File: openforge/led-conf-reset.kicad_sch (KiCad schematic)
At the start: 48 parts, among them Q1 DDC114YU-7-F, Q2 DDC114YU-7-F

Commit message: added footprint associations
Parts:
- R55, R56, R57, R58, R59, R60, R61, R62, R63, R64, R65, R66, R67, R68, R69, R70, R71, R72, R73, R74, R75, R76, R77, R78, R79, R80, R81, R82, R83, R84, R85, R86, R87, R88, R89, R90, R91, R92, R93, R94, R95: footprint (none) -> Resistor_SMD:R_0402_1005Metric
- S2: footprint (none) -> footprints:KMR2xxG_CNK
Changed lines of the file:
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@@
 			)
 		)
-		(property "Footprint" ""
+		(property "Footprint" "Resistor_SMD:R_0402_1005Metric"
 			(at 328.93 93.472 90)
 			(effects
@@
 			)
 		)
-		(property "Footprint" ""
+		(property "Footprint" "Resistor_SMD:R_0402_1005Metric"
 			(at 100.838 119.38 90)
 			(effects
@@
 			)
 		)
-		(property "Footprint" ""
+		(property "Footprint" "Resistor_SMD:R_0402_1005Metric"
 			(at 108.712 46.99 90)
 			(effects
@@
 			)
 		)
-		(property "Footprint" ""
+		(property "Footprint" "Resistor_SMD:R_0402_1005Metric"
 			(at 66.802 46.99 90)
 			(effects
@@
 			)
 		)
-		(property "Footprint" ""
+		(property "Footprint" "Resistor_SMD:R_0402_1005Metric"
 			(at 93.472 46.99 90)
 			(effects
@@
 			)
 		)
-		(property "Footprint" ""
+		(property "Footprint" "Resistor_SMD:R_0402_1005Metric"
 			(at 120.142 46.99 90)
 			(effects
@@
 			)
 		)
-		(property "Footprint" ""
+		(property "Footprint" "Resistor_SMD:R_0402_1005Metric"
 			(at 74.168 119.38 90)
 			(effects
@@
 			)
 		)
-		(property "Footprint" ""
+		(property "Footprint" "Resistor_SMD:R_0402_1005Metric"
 			(at 116.332 46.99 90)
 			(effects
@@
 			)
 		)
-		(property "Footprint" ""
+		(property "Footprint" "Resistor_SMD:R_0402_1005Metric"
 			(at 116.078 119.38 90)
 			(effects
@@
 			)
 		)
-		(property "Footprint" ""
+		(property "Footprint" "Resistor_SMD:R_0402_1005Metric"
 			(at 82.042 46.99 90)
 			(effects
@@
 			)
 		)
-		(property "Footprint" ""
+		(property "Footprint" "Resistor_SMD:R_0402_1005Metric"
 			(at 127.508 119.38 90)
 			(effects
@@
 			)
 		)
-		(property "Footprint" ""
+		(property "Footprint" "Resistor_SMD:R_0402_1005Metric"
 			(at 292.862 48.26 90)
 			(effects
@@
 			)
 		)
-		(property "Footprint" ""
+		(property "Footprint" "Resistor_SMD:R_0402_1005Metric"
 			(at 89.662 46.99 90)
 			(effects
@@
 			)
 		)
-		(property "Footprint" ""
+		(property "Footprint" "Resistor_SMD:R_0402_1005Metric"
 			(at 252.73 97.028 90)
 			(effects
@@
 			)
 		)
-		(property "Footprint" ""
+		(property "Footprint" "Resistor_SMD:R_0402_1005Metric"
 			(at 119.888 119.38 90)
 			(effects
@@
 			)
 		)
-		(property "Footprint" ""
+		(property "Footprint" "Resistor_SMD:R_0402_1005Metric"
 			(at 112.522 46.99 90)
 			(effects
@@
 			)
 		)
-		(property "Footprint" ""
+		(property "Footprint" "Resistor_SMD:R_0402_1005Metric"
 			(at 112.268 119.38 90)
 			(effects
@@
 			)
 		)
-		(property "Footprint" ""
+		(property "Footprint" "Resistor_SMD:R_0402_1005Metric"
 			(at 369.062 48.26 90)
 			(effects
@@
 			)
 		)
-		(property "Footprint" ""
+		(property "Footprint" "footprints:KMR2xxG_CNK"
 			(at 185.42 52.07 0)
 			(effects
@@
 			)
 		)
-		(property "Footprint" ""
+		(property "Footprint" "Resistor_SMD:R_0402_1005Metric"
 			(at 168.91 61.468 90)
 			(effects
@@
 			)
 		)
-		(property "Footprint" ""
+		(property "Footprint" "Resistor_SMD:R_0402_1005Metric"
 			(at 290.83 97.028 90)
 			(effects
@@
 			)
 		)
-		(property "Footprint" ""
+		(property "Footprint" "Resistor_SMD:R_0402_1005Metric"
 			(at 101.092 46.99 90)
 			(effects
@@
 			)
 		)
-		(property "Footprint" ""
+		(property "Footprint" "Resistor_SMD:R_0402_1005Metric"
 			(at 104.902 46.99 90)
 			(effects
@@
 			)
 		)
-		(property "Footprint" ""
+		(property "Footprint" "Resistor_SMD:R_0402_1005Metric"
 			(at 81.788 119.38 90)
 			(effects
@@
 			)
 		)
-		(property "Footprint" ""
+		(property "Footprint" "Resistor_SMD:R_0402_1005Metric"
 			(at 123.698 119.38 90)
 			(effects
@@
 			)
 		)
-		(property "Footprint" ""
+		(property "Footprint" "Resistor_SMD:R_0402_1005Metric"
 			(at 70.612 46.99 90)
 			(effects
@@
 			)
 		)
-		(property "Footprint" ""
+		(property "Footprint" "Resistor_SMD:R_0402_1005Metric"
 			(at 108.458 119.38 90)
 			(effects
@@
 			)
 		)
-		(property "Footprint" ""
+		(property "Footprint" "Resistor_SMD:R_0402_1005Metric"
 			(at 85.852 46.99 90)
 			(effects
@@
 			)
 		)
-		(property "Footprint" ""
+		(property "Footprint" "Resistor_SMD:R_0402_1005Metric"
 			(at 85.598 119.38 90)
 			(effects
@@
 			)
 		)
-		(property "Footprint" ""
+		(property "Footprint" "Resistor_SMD:R_0402_1005Metric"
 			(at 123.952 46.99 90)
 			(effects
@@
 			)
 		)
-		(property "Footprint" ""
+		(property "Footprint" "Resistor_SMD:R_0402_1005Metric"
 			(at 93.218 119.38 90)
 			(effects
@@
 			)
 		)
-		(property "Footprint" ""
+		(property "Footprint" "Resistor_SMD:R_0402_1005Metric"
 			(at 70.358 119.38 90)
 			(effects
@@
 			)
 		)
-		(property "Footprint" ""
+		(property "Footprint" "Resistor_SMD:R_0402_1005Metric"
 			(at 330.962 48.26 90)
 			(effects
@@
 			)
 		)
-		(property "Footprint" ""
+		(property "Footprint" "Resistor_SMD:R_0402_1005Metric"
 			(at 74.422 46.99 90)
 			(effects
@@
 			)
 		)
-		(property "Footprint" ""
+		(property "Footprint" "Resistor_SMD:R_0402_1005Metric"
 			(at 367.03 93.472 90)
 			(effects
@@
 			)
 		)
-		(property "Footprint" ""
+		(property "Footprint" "Resistor_SMD:R_0402_1005Metric"
 			(at 97.028 119.38 90)
 			(effects
@@
 			)
 		)
-		(property "Footprint" ""
+		(property "Footprint" "Resistor_SMD:R_0402_1005Metric"
 			(at 104.648 119.38 90)
 			(effects
@@
 			)
 		)
-		(property "Footprint" ""
+		(property "Footprint" "Resistor_SMD:R_0402_1005Metric"
 			(at 97.282 46.99 90)
 			(effects
@@
 			)
 		)
-		(property "Footprint" ""
+		(property "Footprint" "Resistor_SMD:R_0402_1005Metric"
 			(at 254.762 48.26 90)
 			(effects
@@
 			)
 		)
-		(property "Footprint" ""
+		(property "Footprint" "Resistor_SMD:R_0402_1005Metric"
 			(at 78.232 46.99 90)
 			(effects
@@
 			)
 		)
-		(property "Footprint" ""
+		(property "Footprint" "Resistor_SMD:R_0402_1005Metric"
 			(at 89.408 119.38 90)
 			(effects
@@
 			)
 		)
-		(property "Footprint" ""
+		(property "Footprint" "Resistor_SMD:R_0402_1005Metric"
 			(at 77.978 119.38 90)
 			(effects

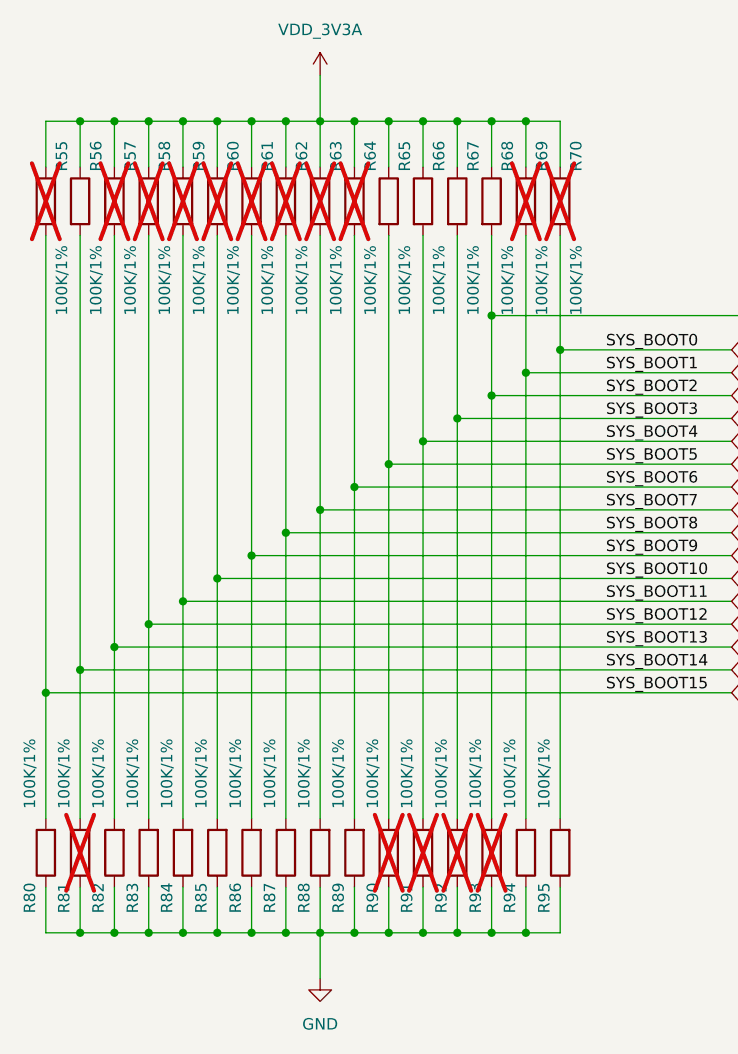
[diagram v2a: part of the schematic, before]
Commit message: fixed all errors and major warnings
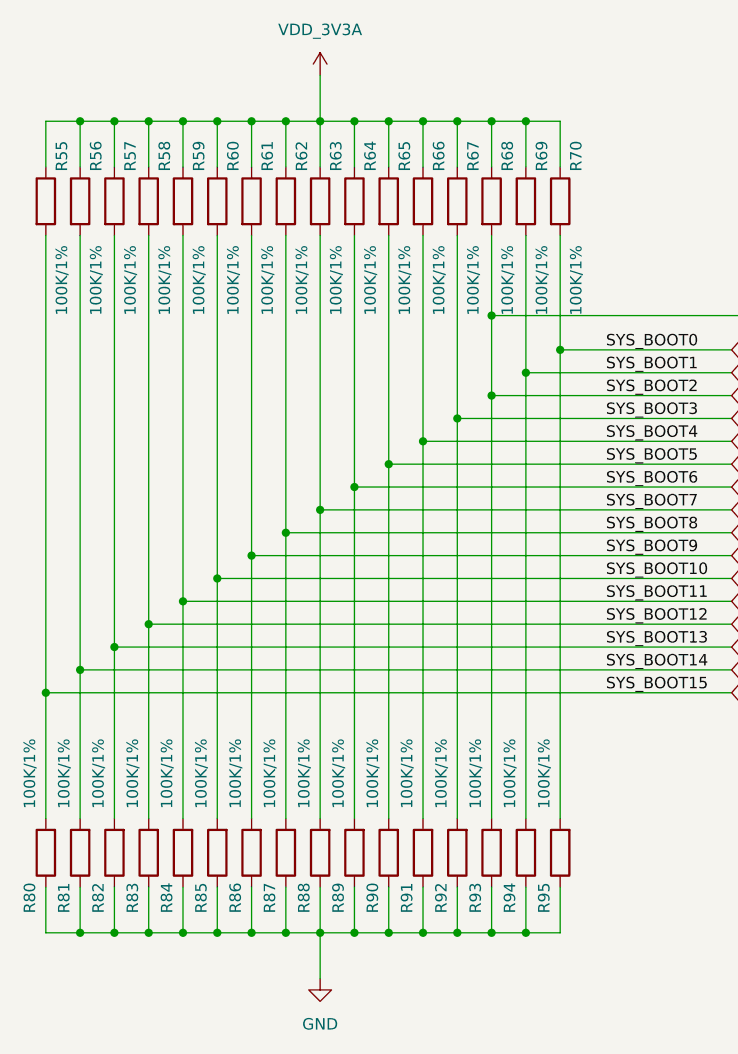
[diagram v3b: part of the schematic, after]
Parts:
- R55, R57, R58, R59, R60, R61, R62, R63, R64, R69, R70, R81, R90, R91, R92, R93: footprint Resistor_SMD:R_0402_1005Metric -> footprints:R_0402_1005Metric; now fitted
- R56, R65, R66, R67, R68, R71, R72, R73, R74, R75, R76, R77, R78, R79, R80, R82, R83, R84, R85, R86, R87, R88, R89, R94, R95: footprint Resistor_SMD:R_0402_1005Metric -> footprints:R_0402_1005Metric
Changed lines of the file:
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@@
 			)
 		)
-		(property "Footprint" "Resistor_SMD:R_0402_1005Metric"
+		(property "Footprint" "footprints:R_0402_1005Metric"
 			(at 328.93 93.472 90)
 			(effects
@@
 			)
 		)
-		(property "Footprint" "Resistor_SMD:R_0402_1005Metric"
+		(property "Footprint" "footprints:R_0402_1005Metric"
 			(at 100.838 119.38 90)
 			(effects
@@
 			)
 		)
-		(property "Footprint" "Resistor_SMD:R_0402_1005Metric"
+		(property "Footprint" "footprints:R_0402_1005Metric"
 			(at 108.712 46.99 90)
 			(effects
@@
 		(in_bom yes)
 		(on_board yes)
-		(dnp yes)
+		(dnp no)
 		(property "Reference" "R55"
 			(at 70.358 43.688 90)
@@
 			)
 		)
-		(property "Footprint" "Resistor_SMD:R_0402_1005Metric"
+		(property "Footprint" "footprints:R_0402_1005Metric"
 			(at 66.802 46.99 90)
 			(effects
@@
 		(in_bom yes)
 		(on_board yes)
-		(dnp yes)
+		(dnp no)
 		(property "Reference" "R62"
 			(at 97.028 43.688 90)
@@
 			)
 		)
-		(property "Footprint" "Resistor_SMD:R_0402_1005Metric"
+		(property "Footprint" "footprints:R_0402_1005Metric"
 			(at 93.472 46.99 90)
 			(effects
@@
 		(in_bom yes)
 		(on_board yes)
-		(dnp yes)
+		(dnp no)
 		(property "Reference" "R69"
 			(at 123.698 43.688 90)
@@
 			)
 		)
-		(property "Footprint" "Resistor_SMD:R_0402_1005Metric"
+		(property "Footprint" "footprints:R_0402_1005Metric"
 			(at 120.142 46.99 90)
 			(effects
@@
 		(in_bom yes)
 		(on_board yes)
-		(dnp yes)
+		(dnp no)
 		(property "Reference" "R81"
 			(at 70.612 122.682 90)
@@
 			)
 		)
-		(property "Footprint" "Resistor_SMD:R_0402_1005Metric"
+		(property "Footprint" "footprints:R_0402_1005Metric"
 			(at 74.168 119.38 90)
 			(effects
@@
 			)
 		)
-		(property "Footprint" "Resistor_SMD:R_0402_1005Metric"
+		(property "Footprint" "footprints:R_0402_1005Metric"
 			(at 116.332 46.99 90)
 			(effects
@@
 		(in_bom yes)
 		(on_board yes)
-		(dnp yes)
+		(dnp no)
 		(property "Reference" "R92"
 			(at 112.522 122.682 90)
@@
 			)
 		)
-		(property "Footprint" "Resistor_SMD:R_0402_1005Metric"
+		(property "Footprint" "footprints:R_0402_1005Metric"
 			(at 116.078 119.38 90)
 			(effects
@@
 		(in_bom yes)
 		(on_board yes)
-		(dnp yes)
+		(dnp no)
 		(property "Reference" "R59"
 			(at 85.598 43.688 90)
@@
 			)
 		)
-		(property "Footprint" "Resistor_SMD:R_0402_1005Metric"
+		(property "Footprint" "footprints:R_0402_1005Metric"
 			(at 82.042 46.99 90)
 			(effects
@@
 			)
 		)
-		(property "Footprint" "Resistor_SMD:R_0402_1005Metric"
+		(property "Footprint" "footprints:R_0402_1005Metric"
 			(at 127.508 119.38 90)
 			(effects
@@
 			)
 		)
-		(property "Footprint" "Resistor_SMD:R_0402_1005Metric"
+		(property "Footprint" "footprints:R_0402_1005Metric"
 			(at 292.862 48.26 90)
 			(effects
@@
 		(in_bom yes)
 		(on_board yes)
-		(dnp yes)
+		(dnp no)
 		(property "Reference" "R61"
 			(at 93.218 43.688 90)
@@
 			)
 		)
-		(property "Footprint" "Resistor_SMD:R_0402_1005Metric"
+		(property "Footprint" "footprints:R_0402_1005Metric"
 			(at 89.662 46.99 90)
 			(effects
@@
 			)
 		)
-		(property "Footprint" "Resistor_SMD:R_0402_1005Metric"
+		(property "Footprint" "footprints:R_0402_1005Metric"
 			(at 252.73 97.028 90)
 			(effects
@@
 		(in_bom yes)
 		(on_board yes)
-		(dnp yes)
+		(dnp no)
 		(property "Reference" "R93"
 			(at 116.332 122.682 90)
@@
 			)
 		)
-		(property "Footprint" "Resistor_SMD:R_0402_1005Metric"
+		(property "Footprint" "footprints:R_0402_1005Metric"
 			(at 119.888 119.38 90)
 			(effects
@@
 			)
 		)
-		(property "Footprint" "Resistor_SMD:R_0402_1005Metric"
+		(property "Footprint" "footprints:R_0402_1005Metric"
 			(at 112.522 46.99 90)
 			(effects
@@
 		(in_bom yes)
 		(on_board yes)
-		(dnp yes)
+		(dnp no)
 		(property "Reference" "R91"
 			(at 108.712 122.682 90)
@@
 			)
 		)
-		(property "Footprint" "Resistor_SMD:R_0402_1005Metric"
+		(property "Footprint" "footprints:R_0402_1005Metric"
 			(at 112.268 119.38 90)
 			(effects
@@
 			)
 		)
-		(property "Footprint" "Resistor_SMD:R_0402_1005Metric"
+		(property "Footprint" "footprints:R_0402_1005Metric"
 			(at 369.062 48.26 90)
 			(effects
@@
 			)
 		)
-		(property "Footprint" "Resistor_SMD:R_0402_1005Metric"
+		(property "Footprint" "footprints:R_0402_1005Metric"
 			(at 168.91 61.468 90)
 			(effects
@@
 			)
 		)
-		(property "Footprint" "Resistor_SMD:R_0402_1005Metric"
+		(property "Footprint" "footprints:R_0402_1005Metric"
 			(at 290.83 97.028 90)
 			(effects
@@
 		(in_bom yes)
 		(on_board yes)
-		(dnp yes)
+		(dnp no)
 		(property "Reference" "R64"
 			(at 104.648 43.688 90)
@@
 			)
 		)
-		(property "Footprint" "Resistor_SMD:R_0402_1005Metric"
+		(property "Footprint" "footprints:R_0402_1005Metric"
 			(at 101.092 46.99 90)
 			(effects
@@
 			)
 		)
-		(property "Footprint" "Resistor_SMD:R_0402_1005Metric"
+		(property "Footprint" "footprints:R_0402_1005Metric"
 			(at 104.902 46.99 90)
 			(effects
@@
 			)
 		)
-		(property "Footprint" "Resistor_SMD:R_0402_1005Metric"
+		(property "Footprint" "footprints:R_0402_1005Metric"
 			(at 81.788 119.38 90)
 			(effects
@@
 			)
 		)
-		(property "Footprint" "Resistor_SMD:R_0402_1005Metric"
+		(property "Footprint" "footprints:R_0402_1005Metric"
 			(at 123.698 119.38 90)
 			(effects
@@
 			)
 		)
-		(property "Footprint" "Resistor_SMD:R_0402_1005Metric"
+		(property "Footprint" "footprints:R_0402_1005Metric"
 			(at 70.612 46.99 90)
 			(effects
@@
 		(in_bom yes)
 		(on_board yes)
-		(dnp yes)
+		(dnp no)
 		(property "Reference" "R90"
 			(at 104.902 122.682 90)
@@
 			)
 		)
-		(property "Footprint" "Resistor_SMD:R_0402_1005Metric"
+		(property "Footprint" "footprints:R_0402_1005Metric"
 			(at 108.458 119.38 90)
 			(effects
@@
 		(in_bom yes)
 		(on_board yes)
-		(dnp yes)
+		(dnp no)
 		(property "Reference" "R60"
 			(at 89.408 43.688 90)
@@
 			)
 		)
-		(property "Footprint" "Resistor_SMD:R_0402_1005Metric"
+		(property "Footprint" "footprints:R_0402_1005Metric"
 			(at 85.852 46.99 90)
 			(effects
@@
 			)
 		)
-		(property "Footprint" "Resistor_SMD:R_0402_1005Metric"
+		(property "Footprint" "footprints:R_0402_1005Metric"
 			(at 85.598 119.38 90)
 			(effects
@@
 		(in_bom yes)
 		(on_board yes)
-		(dnp yes)
+		(dnp no)
 		(property "Reference" "R70"
 			(at 127.508 43.688 90)
@@
 			)
 		)
-		(property "Footprint" "Resistor_SMD:R_0402_1005Metric"
+		(property "Footprint" "footprints:R_0402_1005Metric"
 			(at 123.952 46.99 90)
 			(effects
@@
 			)
 		)
-		(property "Footprint" "Resistor_SMD:R_0402_1005Metric"
+		(property "Footprint" "footprints:R_0402_1005Metric"
 			(at 93.218 119.38 90)
 			(effects
@@
 			)
 		)
-		(property "Footprint" "Resistor_SMD:R_0402_1005Metric"
+		(property "Footprint" "footprints:R_0402_1005Metric"
 			(at 70.358 119.38 90)
 			(effects
@@
 			)
 		)
-		(property "Footprint" "Resistor_SMD:R_0402_1005Metric"
+		(property "Footprint" "footprints:R_0402_1005Metric"
 			(at 330.962 48.26 90)
 			(effects
@@
 		(in_bom yes)
 		(on_board yes)
-		(dnp yes)
+		(dnp no)
 		(property "Reference" "R57"
 			(at 77.978 43.688 90)
@@
 			)
 		)
-		(property "Footprint" "Resistor_SMD:R_0402_1005Metric"
+		(property "Footprint" "footprints:R_0402_1005Metric"
 			(at 74.422 46.99 90)
 			(effects
@@
 			)
 		)
-		(property "Footprint" "Resistor_SMD:R_0402_1005Metric"
+		(property "Footprint" "footprints:R_0402_1005Metric"
 			(at 367.03 93.472 90)
 			(effects
@@
 			)
 		)
-		(property "Footprint" "Resistor_SMD:R_0402_1005Metric"
+		(property "Footprint" "footprints:R_0402_1005Metric"
 			(at 97.028 119.38 90)
 			(effects
@@
 			)
 		)
-		(property "Footprint" "Resistor_SMD:R_0402_1005Metric"
+		(property "Footprint" "footprints:R_0402_1005Metric"
 			(at 104.648 119.38 90)
 			(effects
@@
 		(in_bom yes)
 		(on_board yes)
-		(dnp yes)
+		(dnp no)
 		(property "Reference" "R63"
 			(at 100.838 43.688 90)
@@
 			)
 		)
-		(property "Footprint" "Resistor_SMD:R_0402_1005Metric"
+		(property "Footprint" "footprints:R_0402_1005Metric"
 			(at 97.282 46.99 90)
 			(effects
@@
 			)
 		)
-		(property "Footprint" "Resistor_SMD:R_0402_1005Metric"
+		(property "Footprint" "footprints:R_0402_1005Metric"
 			(at 254.762 48.26 90)
 			(effects
@@
 		(in_bom yes)
 		(on_board yes)
-		(dnp yes)
+		(dnp no)
 		(property "Reference" "R58"
 			(at 81.788 43.688 90)
@@
 			)
 		)
-		(property "Footprint" "Resistor_SMD:R_0402_1005Metric"
+		(property "Footprint" "footprints:R_0402_1005Metric"
 			(at 78.232 46.99 90)
 			(effects
@@
 			)
 		)
-		(property "Footprint" "Resistor_SMD:R_0402_1005Metric"
+		(property "Footprint" "footprints:R_0402_1005Metric"
 			(at 89.408 119.38 90)
 			(effects
@@
 			)
 		)
-		(property "Footprint" "Resistor_SMD:R_0402_1005Metric"
+		(property "Footprint" "footprints:R_0402_1005Metric"
 			(at 77.978 119.38 90)
 			(effects
